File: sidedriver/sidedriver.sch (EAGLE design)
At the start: 30 parts, among them IC2 LT1086CM-3.3, Q1 8MHz

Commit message: sidedriver: PCB rev.2 created
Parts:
- removed C10: i tu tez, rcl:C-EUC0603
- removed SV2: (no value), con-lstb:MA07-1
- added C11: 100n, rcl:C-EUC0603
- added R1: 100k, rcl:R-EU_R0603
- added RST: TACT_SWITCH, wb_2:TACT_SWITCH
- added SV1: (no value), con-lstb:MA08-1
- C2: value i tu tez -> 10u; device rcl:C-EUC0603 -> rcl:CPOL-EUSMCA
- C3: value wartosc, tej -> 10u; device rcl:C-EUC0603 -> rcl:CPOL-EUSMCA
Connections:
- new net N$2: U$1.PB6
- new net N$3: U$1.PB7
- new net N$6: U$1.PA11
- new net N$7: U$1.PA8
- net !RST: now also C11.2, R1.2, RST.S
- net +12V: now also SV1.1; no longer SV2.7
- net +3V3: now also C3.+, R1.1, SV1.7; no longer C10.1, C2.1
- net +5V: now also C2.+, SV1.8; no longer C3.1, SV2.1
- net GND: now also C11.1, C2.-, C3.-, RST.P, SV1.6; no longer C10.2, C2.2, C3.2, SV2.2
- net G_ADC1: now also SV1.5; no longer SV2.3
- net G_ADC2: now also SV1.4; no longer SV2.4
- net LED-PWM: now also U$1.PA7; no longer U$1.PC9
- net M1-ENB: now also U$1.PA0; no longer U$1.PA3
- net M2-CS: now also U$1.PC5; no longer U$1.PA7
- net SRV1: now also SV1.3, U$1.PB15; no longer SV2.5, U$1.PA8
- net SRV2: now also SV1.2, U$1.PB14; no longer SV2.6, U$1.PA11
- net TRANS: now also U$1.PA3; no longer U$1.PC8
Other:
- note added: "(TIM12_CH1)"
- note added: "(TIM12_CH2)"
- note added: "(TIM8_CH1)"
- note added: "(TIM8_CH2)"
- note removed: "(TIM3_CH1)"
- note removed: "(TIM3_CH2)"
- note removed: "(TIM3_CH4)"

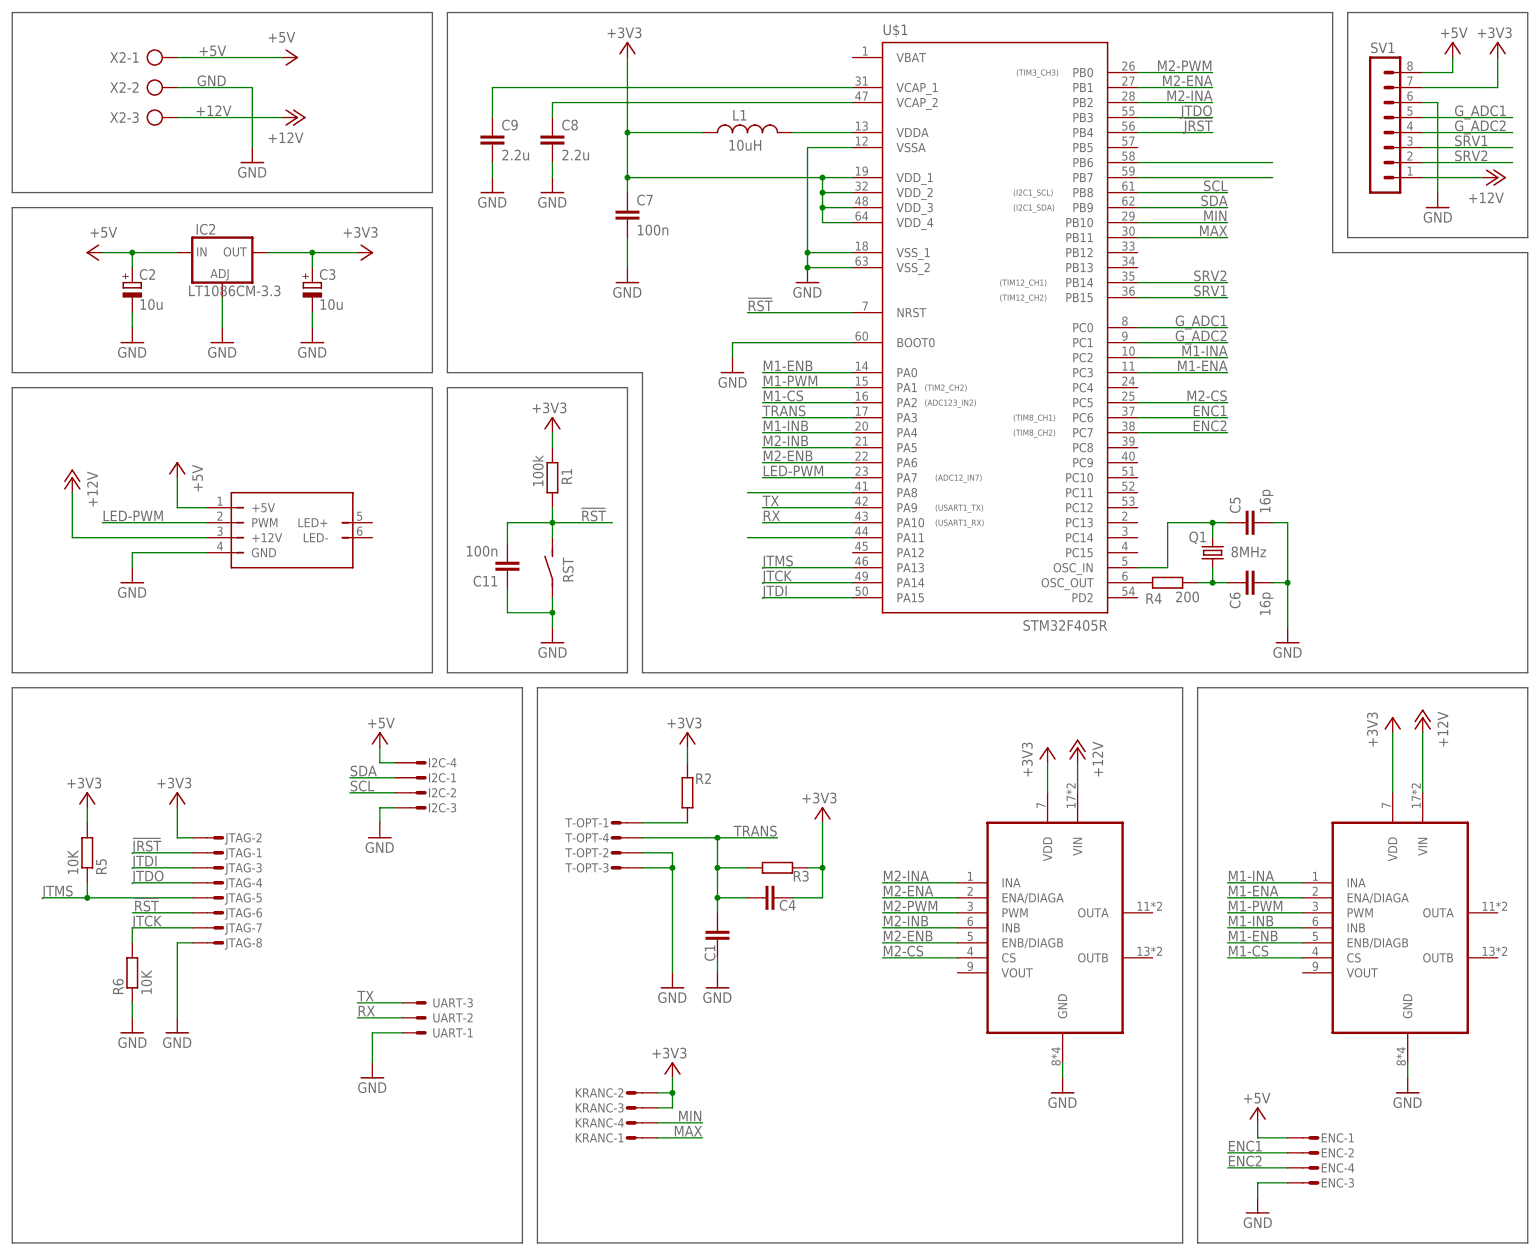
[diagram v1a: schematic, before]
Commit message: sidedriver: PCB rev.2 updates
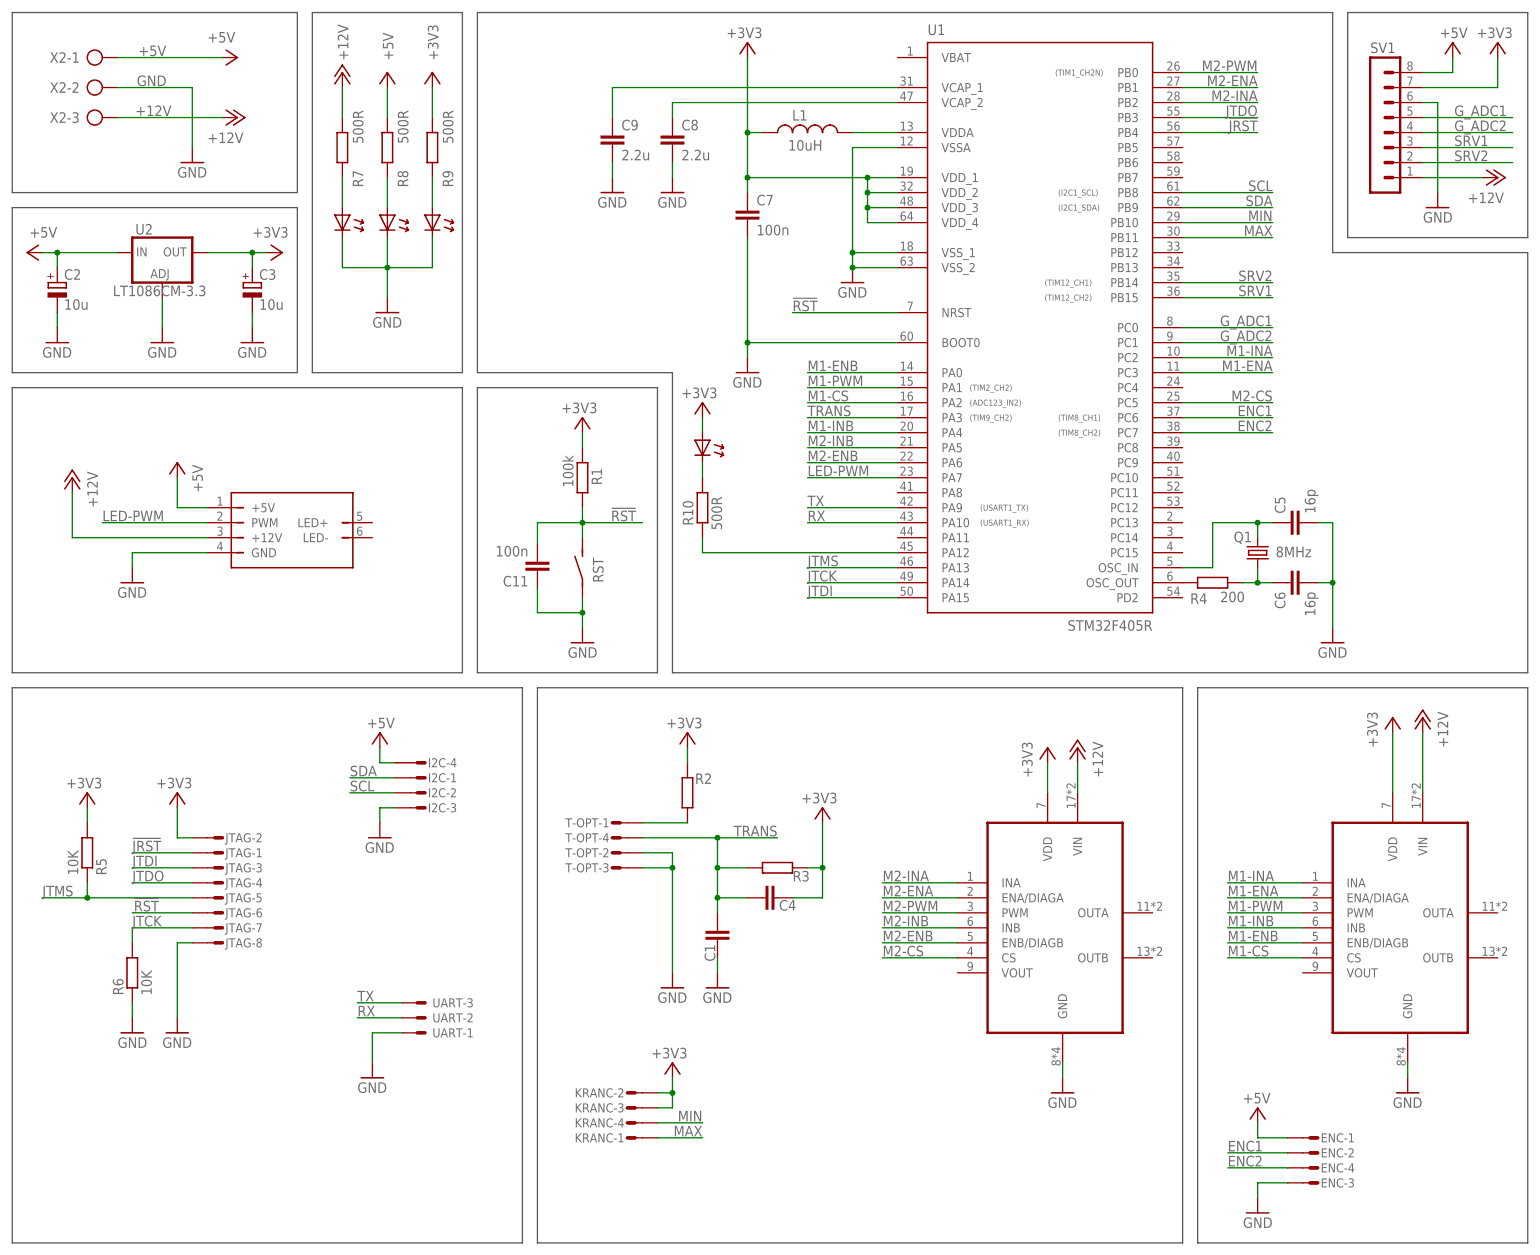
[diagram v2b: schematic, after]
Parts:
- removed IC2: LT1086CM-3.3, v-reg:LD117AD2MTR
- removed U$1: STM32F405R, stm32f4:STM32F405R
- added R10, R7, R8, R9: 500R, rcl:R-EU_R0603
- added U$6, U$7, U$8, U$9: LED0603, wb:LED0603
- added U1: STM32F405R, stm32f4:STM32F405R
- added U2: LT1086CM-3.3, v-reg:LD117AD2MTR
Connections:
- removed net N$2: U$1.PB6
- removed net N$3: U$1.PB7
- removed net N$6: U$1.PA11
- removed net N$7: U$1.PA8
- new net N$10: R9.2, U$8.A
- new net N$11: R10.2, U$9.C
- new net N$12: R10.1, U1.PA12
- new net N$8: R7.2, U$6.A
- new net N$9: R8.2, U$7.A
- net !JRST: now also U1.PB4; no longer U$1.PB4
- net !RST: now also U1.NRST; no longer U$1.NRST
- net +12V: now also R7.1
- net +3V3: now also R9.1, U$9.A, U1.VDD_1, U1.VDD_2, U1.VDD_3, U1.VDD_4, U2.OUT; no longer IC2.OUT, U$1.VDD_1, U$1.VDD_2, U$1.VDD_3, U$1.VDD_4
- net +5V: now also R8.1, U2.IN; no longer IC2.IN
- net ENC1: now also U1.PC6; no longer U$1.PC6
- net ENC2: now also U1.PC7; no longer U$1.PC7
- net GND: now also U$6.C, U$7.C, U$8.C, U1.BOOT0, U1.VSSA, U1.VSS_1, U1.VSS_2, U2.ADJ; no longer IC2.ADJ, U$1.BOOT0, U$1.VSSA, U$1.VSS_1, U$1.VSS_2
- net G_ADC1: now also U1.PC0; no longer U$1.PC0
- net G_ADC2: now also U1.PC1; no longer U$1.PC1
- net JTCK: now also U1.PA14; no longer U$1.PA14
- net JTDI: now also U1.PA15; no longer U$1.PA15
- net JTDO: now also U1.PB3; no longer U$1.PB3
- net JTMS: now also U1.PA13; no longer U$1.PA13
- net LED-PWM: now also U1.PA7; no longer U$1.PA7
- net M1-CS: now also U1.PA2; no longer U$1.PA2
- net M1-ENA: now also U1.PC3; no longer U$1.PC3
- net M1-ENB: now also U1.PA0; no longer U$1.PA0
- net M1-INA: now also U1.PC2; no longer U$1.PC2
- net M1-INB: now also U1.PA4; no longer U$1.PA4
- net M1-PWM: now also U1.PA1; no longer U$1.PA1
- net M2-CS: now also U1.PC5; no longer U$1.PC5
- net M2-ENA: now also U1.PB1; no longer U$1.PB1
- net M2-ENB: now also U1.PA6; no longer U$1.PA6
- net M2-INA: now also U1.PB2; no longer U$1.PB2
- net M2-INB: now also U1.PA5; no longer U$1.PA5
- net M2-PWM: now also U1.PB0; no longer U$1.PB0
- net MAX: now also U1.PB11; no longer U$1.PB11
- net MIN: now also U1.PB10; no longer U$1.PB10
- net N$20: now also U1.VDDA; no longer U$1.VDDA
- net N$22: now also U1.OSC_OUT; no longer U$1.OSC_OUT
- net N$23: now also U1.VCAP_2; no longer U$1.VCAP_2
- net N$24: now also U1.VCAP_1; no longer U$1.VCAP_1
- net N$5: now also U1.OSC_IN; no longer U$1.OSC_IN
- net RX: now also U1.PA10; no longer U$1.PA10
- net SCL: now also U1.PB8; no longer U$1.PB8
- net SDA: now also U1.PB9; no longer U$1.PB9
- net SRV1: now also U1.PB15; no longer U$1.PB15
- net SRV2: now also U1.PB14; no longer U$1.PB14
- net TRANS: now also U1.PA3; no longer U$1.PA3
- net TX: now also U1.PA9; no longer U$1.PA9
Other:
- note added: "(TIM1_CH2N)"
- note added: "(TIM9_CH2)"
- note removed: "(ADC12_IN7)"
- note removed: "(TIM3_CH3)"
- moved on the sheet: C11, C2, C3, C5, C6, C7, C8, C9, L1, Q1, R1, R4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
